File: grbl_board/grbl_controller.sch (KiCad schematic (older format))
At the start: 32 parts, among them J3 USB_B, J4 ICSP, SW1 SW_Push, U1 FT231XS, U2 ATmega2560-16AU, Y1 16M

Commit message: complete footprint associations
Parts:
- D1, D2: footprint (none) -> LED_SMD:LED_1206_3216Metric_Pad1.42x1.75mm_HandSolder; Digikey Part No. (none) -> 404-1042-1-ND
- U2: Digikey Part No. (none) -> ATMEGA2560-16AU-ND
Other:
- note added: "RXLED"
- note added: "TXLED"
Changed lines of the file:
@@
 F 2 "Package_QFP:TQFP-100_14x14mm_P0.5mm" H 5950 4000 50  0001 C CIN
 F 3 "http://ww1.microchip.com/downloads/en/DeviceDoc/Atmel-2549-8-bit-AVR-Microcontroller-ATmega640-1280-1281-2560-2561_datasheet.pdf" H 5950 4000 50  0001 C CNN
+F 4 "ATMEGA2560-16AU-ND" H 5950 4000 50  0001 C CNN "Digikey Part No."
 	1    5950 4000
 	1    0    0    -1
@@
 F 0 "D1" V 4047 6380 50  0000 L CNN
 F 1 "LED" V 4138 6380 50  0000 L CNN
-F 2 "" H 4100 6300 50  0001 C CNN
-F 3 "~" H 4100 6300 50  0001 C CNN
+F 2 "LED_SMD:LED_1206_3216Metric_Pad1.42x1.75mm_HandSolder" H 4100 6300 50  0001 C CNN
+F 3 "https://media.digikey.com/pdf/Data%20Sheets/Stanley%20Electric%20PDFs/1101W_Series.pdf" H 4100 6300 50  0001 C CNN
+F 4 "404-1042-1-ND" H 4100 6300 50  0001 C CNN "Digikey Part No."
 	1    4100 6300
 	0    1    1    0
@@
 F 0 "D2" V 4397 6380 50  0000 L CNN
 F 1 "LED" V 4488 6380 50  0000 L CNN
-F 2 "" H 4450 6300 50  0001 C CNN
-F 3 "~" H 4450 6300 50  0001 C CNN
+F 2 "LED_SMD:LED_1206_3216Metric_Pad1.42x1.75mm_HandSolder" H 4450 6300 50  0001 C CNN
+F 3 "https://media.digikey.com/pdf/Data%20Sheets/Stanley%20Electric%20PDFs/1101W_Series.pdf" H 4450 6300 50  0001 C CNN
+F 4 "404-1042-1-ND" H 4450 6300 50  0001 C CNN "Digikey Part No."
 	1    4450 6300
 	0    1    1    0
@@
 Wire Wire Line
 	9000 3850 9400 3850
+Text Notes 4500 6100 0    50   ~ 0
+TXLED
+Text Notes 4150 6100 0    50   ~ 0
+RXLED
 $EndSCHEMATC

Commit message: routing done
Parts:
- J3: symbol grbl_board-rescue:USB_B-Connector -> Connector:USB_B
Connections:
- net GND: no longer R3.1, R3.2
- net at C7.1, U2.33 (XTAL2), Y1.3: now also R3.2
- net at C6.1, U2.34 (XTAL1), Y1.1: now also R3.1
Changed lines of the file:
@@
 $EndComp
-Wire Wire Line
-	2700 1550 2700 1450
-Wire Wire Line
-	2700 1450 3100 1450
-Connection ~ 3100 1450
 Wire Wire Line
 	3100 2000 3100 1700
-Wire Wire Line
-	2700 1850 2700 2000
-Wire Wire Line
-	2700 2000 3100 2000
 $Comp
 L power:+5V #PWR016
@@
 $EndComp
 $Comp
-L grbl_board-rescue:USB_B-Connector J?
+L Connector:USB_B J?
 U 1 1 61809DB5
 P 1350 4000
@@
 Text Notes 4150 6100 0    50   ~ 0
 RXLED
+Wire Wire Line
+	4000 2000 4000 2350
+Wire Wire Line
+	4000 2350 2700 2350
+Wire Wire Line
+	2700 1850 2700 2350
+Wire Wire Line
+	4000 1450 4000 1100
+Wire Wire Line
+	4000 1100 2700 1100
+Wire Wire Line
+	2700 1100 2700 1550
 $EndSCHEMATC

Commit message: added usb 3d model and fixed footprint associations
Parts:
- J3: footprint Connector_USB:USB_B_OST_USB-B1HSxx_Horizontal -> grbl_board:USB_B_OST_USB-B1HSxx_Horizontal
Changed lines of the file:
@@
 F 0 "J3" H 1407 4467 50  0000 C CNN
 F 1 "USB_B" H 1407 4376 50  0000 C CNN
-F 2 "Connector_USB:USB_B_OST_USB-B1HSxx_Horizontal" H 1500 3950 50  0001 C CNN
+F 2 "grbl_board:USB_B_OST_USB-B1HSxx_Horizontal" H 1500 3950 50  0001 C CNN
 F 3 "https://belfuse.com/resources/datasheets/stewartconnector/ds-stw-usb-2.0-type-b-connectors.pdf" H 1500 3950 50  0001 C CNN
 F 4 "380-1492-ND" H 1350 4000 50  0001 C CNN "Digikey Part No."

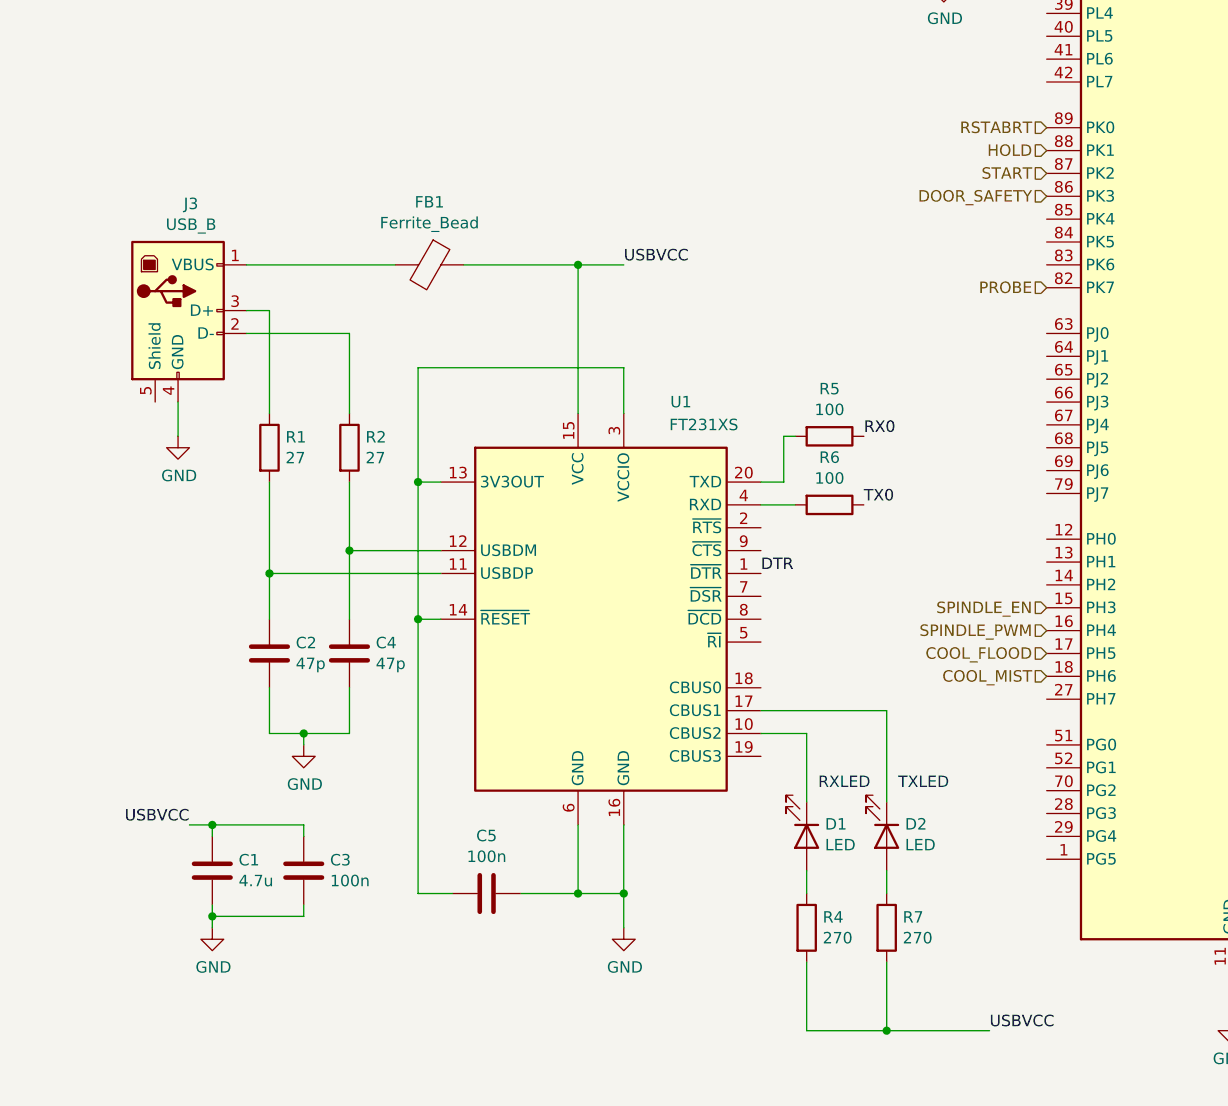
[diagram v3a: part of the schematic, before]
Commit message: added some descriptions in the schematic and added gerber file
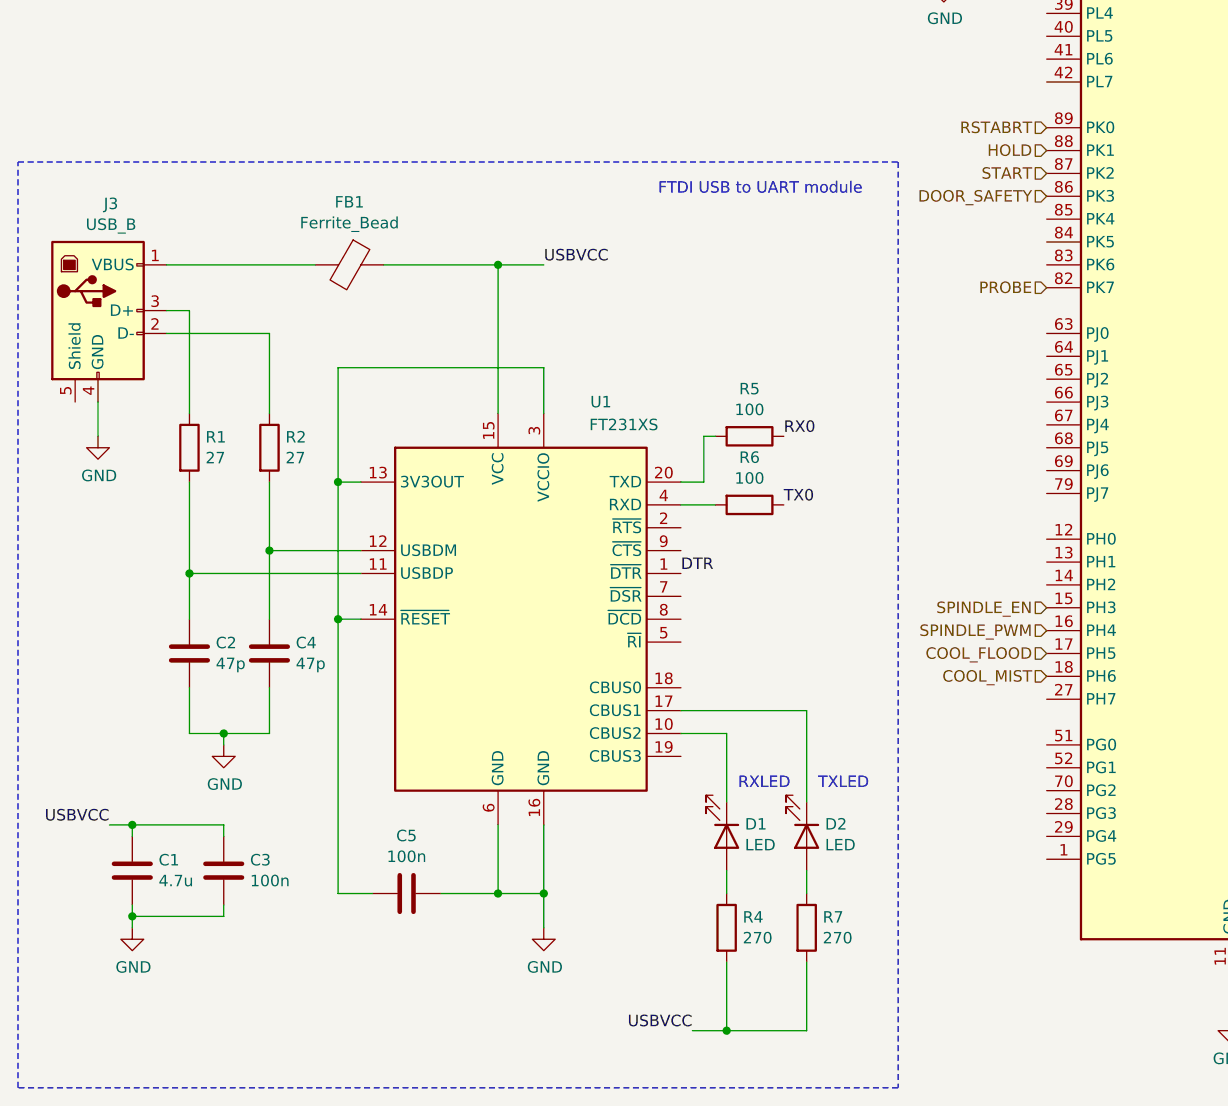
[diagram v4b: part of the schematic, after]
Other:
- note added: "FTDI USB to UART module"
- moved on the sheet: C1, C2, C3, C4, C5, D1, D2, FB1, J3, R1, R2, R4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

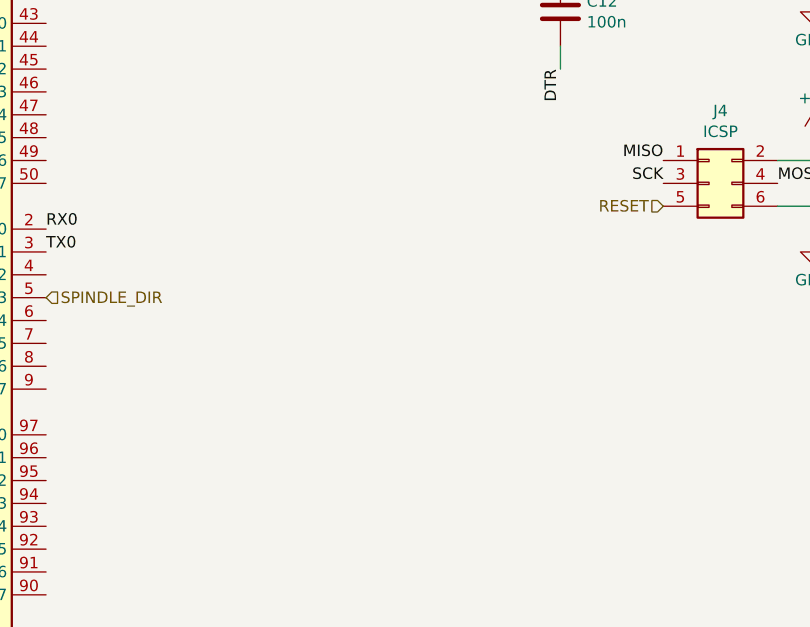
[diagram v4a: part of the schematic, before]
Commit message: added limit switch indicator LEDs
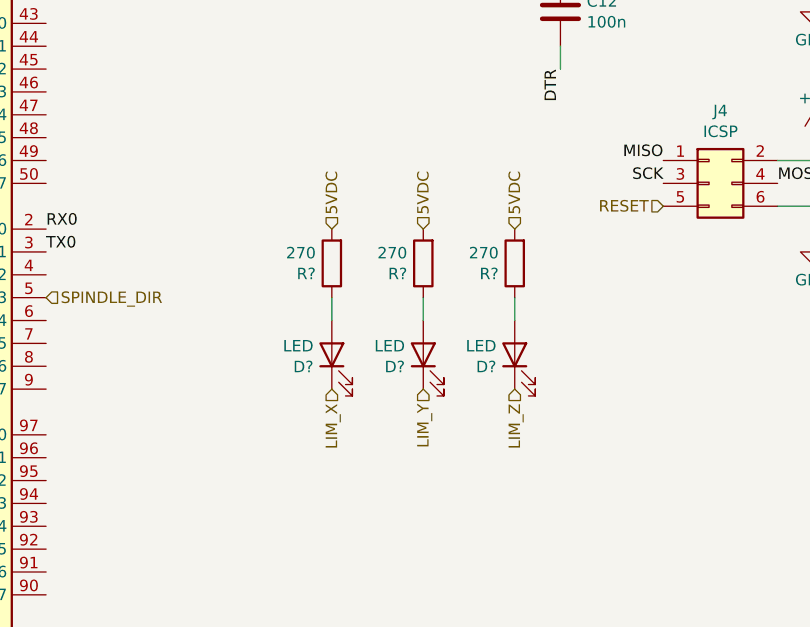
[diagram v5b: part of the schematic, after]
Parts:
- added D? (x3): LED, LED_SMD:LED_1206_3216Metric_Pad1.42x1.75mm_HandSolder, symbol Device:LED
- added R? (x3): 270, Resistor_SMD:R_0805_2012Metric_Pad1.15x1.40mm_HandSolder, symbol Device:R
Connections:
- net LIM_X: now also D?.1 (K)
- net LIM_Y: now also D?.1 (K)
- net LIM_Z: now also D?.1 (K)
- new net: D?.2 (A), R?.1 (x3)
- new net 5VDC: R?.2, R?.2, R?.2
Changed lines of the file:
@@
 Text Notes 3450 3500 0    50   ~ 0
 FTDI USB to UART module
+Text HLabel 8800 5000 1    50   Input ~ 0
+5VDC
+$Comp
+L Device:LED D?
+U 1 1 61CDF7A9
+P 8800 5550
+AR Path="/61764E0B/61CDF7A9" Ref="D?"  Part="1"
+AR Path="/619755E7/61CDF7A9" Ref="D?"  Part="1"
+AR Path="/61D39570/61CDF7A9" Ref="D?"  Part="1"
+F 0 "D?" V 8747 5630 50  0000 L CNN
+F 1 "LED" V 8838 5630 50  0000 L CNN
+F 2 "LED_SMD:LED_1206_3216Metric_Pad1.42x1.75mm_HandSolder" H 8800 5550 50  0001 C CNN
+F 3 "https://media.digikey.com/pdf/Data%20Sheets/Stanley%20Electric%20PDFs/1101W_Series.pdf" H 8800 5550 50  0001 C CNN
+F 4 "404-1046-1-ND" H 8800 5550 50  0001 C CNN "Digikey Part No."
+	1    8800 5550
+	0    -1   -1   0
+$EndComp
+$Comp
+L Device:R R?
+U 1 1 61CDF7B0
+P 8800 5150
+AR Path="/61764E0B/61CDF7B0" Ref="R?"  Part="1"
+AR Path="/619755E7/61CDF7B0" Ref="R?"  Part="1"
+AR Path="/61D39570/61CDF7B0" Ref="R?"  Part="1"
+F 0 "R?" H 8870 5196 50  0000 L CNN
+F 1 "270" H 8870 5105 50  0000 L CNN
+F 2 "Resistor_SMD:R_0805_2012Metric_Pad1.15x1.40mm_HandSolder" V 8730 5150 50  0001 C CNN
+F 3 "https://www.yageo.com/upload/media/product/productsearch/datasheet/rchip/PYu-SR_20105_RoHS_L_9.pdf" H 8800 5150 50  0001 C CNN
+F 4 "YAG6172CT-ND" H 8800 5150 50  0001 C CNN "Digikey Part No."
+	1    8800 5150
+	-1   0    0    1
+$EndComp
+Wire Wire Line
+	8800 5300 8800 5400
+Text HLabel 8400 5000 1    50   Input ~ 0
+5VDC
+$Comp
+L Device:LED D?
+U 1 1 61CDF7B9
+P 8400 5550
+AR Path="/61764E0B/61CDF7B9" Ref="D?"  Part="1"
+AR Path="/619755E7/61CDF7B9" Ref="D?"  Part="1"
+AR Path="/61D39570/61CDF7B9" Ref="D?"  Part="1"
+F 0 "D?" V 8347 5630 50  0000 L CNN
+F 1 "LED" V 8438 5630 50  0000 L CNN
+F 2 "LED_SMD:LED_1206_3216Metric_Pad1.42x1.75mm_HandSolder" H 8400 5550 50  0001 C CNN
+F 3 "https://media.digikey.com/pdf/Data%20Sheets/Stanley%20Electric%20PDFs/1101W_Series.pdf" H 8400 5550 50  0001 C CNN
+F 4 "404-1046-1-ND" H 8400 5550 50  0001 C CNN "Digikey Part No."
+	1    8400 5550
+	0    -1   -1   0
+$EndComp
+$Comp
+L Device:R R?
+U 1 1 61CDF7C0
+P 8400 5150
+AR Path="/61764E0B/61CDF7C0" Ref="R?"  Part="1"
+AR Path="/619755E7/61CDF7C0" Ref="R?"  Part="1"
+AR Path="/61D39570/61CDF7C0" Ref="R?"  Part="1"
+F 0 "R?" H 8470 5196 50  0000 L CNN
+F 1 "270" H 8470 5105 50  0000 L CNN
+F 2 "Resistor_SMD:R_0805_2012Metric_Pad1.15x1.40mm_HandSolder" V 8330 5150 50  0001 C CNN
+F 3 "https://www.yageo.com/upload/media/product/productsearch/datasheet/rchip/PYu-SR_20105_RoHS_L_9.pdf" H 8400 5150 50  0001 C CNN
+F 4 "YAG6172CT-ND" H 8400 5150 50  0001 C CNN "Digikey Part No."
+	1    8400 5150
+	-1   0    0    1
+$EndComp
+Wire Wire Line
+	8400 5300 8400 5400
+Wire Wire Line
+	8000 5300 8000 5400
+$Comp
+L Device:R R?
+U 1 1 61CDF7C9
+P 8000 5150
+AR Path="/61764E0B/61CDF7C9" Ref="R?"  Part="1"
+AR Path="/619755E7/61CDF7C9" Ref="R?"  Part="1"
+AR Path="/61D39570/61CDF7C9" Ref="R?"  Part="1"
+F 0 "R?" H 8070 5196 50  0000 L CNN
+F 1 "270" H 8070 5105 50  0000 L CNN
+F 2 "Resistor_SMD:R_0805_2012Metric_Pad1.15x1.40mm_HandSolder" V 7930 5150 50  0001 C CNN
+F 3 "https://www.yageo.com/upload/media/product/productsearch/datasheet/rchip/PYu-SR_20105_RoHS_L_9.pdf" H 8000 5150 50  0001 C CNN
+F 4 "YAG6172CT-ND" H 8000 5150 50  0001 C CNN "Digikey Part No."
+	1    8000 5150
+	-1   0    0    1
+$EndComp
+$Comp
+L Device:LED D?
+U 1 1 61CDF7D0
+P 8000 5550
+AR Path="/61764E0B/61CDF7D0" Ref="D?"  Part="1"
+AR Path="/619755E7/61CDF7D0" Ref="D?"  Part="1"
+AR Path="/61D39570/61CDF7D0" Ref="D?"  Part="1"
+F 0 "D?" V 7947 5630 50  0000 L CNN
+F 1 "LED" V 8038 5630 50  0000 L CNN
+F 2 "LED_SMD:LED_1206_3216Metric_Pad1.42x1.75mm_HandSolder" H 8000 5550 50  0001 C CNN
+F 3 "https://media.digikey.com/pdf/Data%20Sheets/Stanley%20Electric%20PDFs/1101W_Series.pdf" H 8000 5550 50  0001 C CNN
+F 4 "404-1046-1-ND" H 8000 5550 50  0001 C CNN "Digikey Part No."
+	1    8000 5550
+	0    -1   -1   0
+$EndComp
+Text HLabel 8000 5000 1    50   Input ~ 0
+5VDC
+Text HLabel 8000 5700 3    50   Input ~ 0
+LIM_X
+Text HLabel 8400 5700 3    50   Input ~ 0
+LIM_Y
+Text HLabel 8800 5700 3    50   Input ~ 0
+LIM_Z
 $EndSCHEMATC
